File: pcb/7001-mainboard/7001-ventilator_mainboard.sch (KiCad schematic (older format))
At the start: 117 parts, among them J1 USB_B_Micro, J10 6-pin header, J11 4-pin screw terminal, J12 3-pin screw terminal, J13 2-pin screw terminal, J14 2-pin screw terminal, J15 2x10-pin header, J16 10-pin SWD header, J2 4-pin header, J3 2-pin screw terminal, J4 DNI, J5 2-pin screw terminal, J6 5V out, J7 2-pin screw terminal, J8 3-pin screw terminal, J9 Raspberry_Pi_2_3, U13 ITS4142NHUMA1, U14 ITS4142NHUMA1, U2 TPD2E2U06, U3 LPC11U37FBD48-401_, U4 MCP1825S-3302E, U5 S24SE05004PDFA_DC-DC, U6 LM2937IMP-12/NOPB, U7 AD5410AREZ, Y1 12MHz

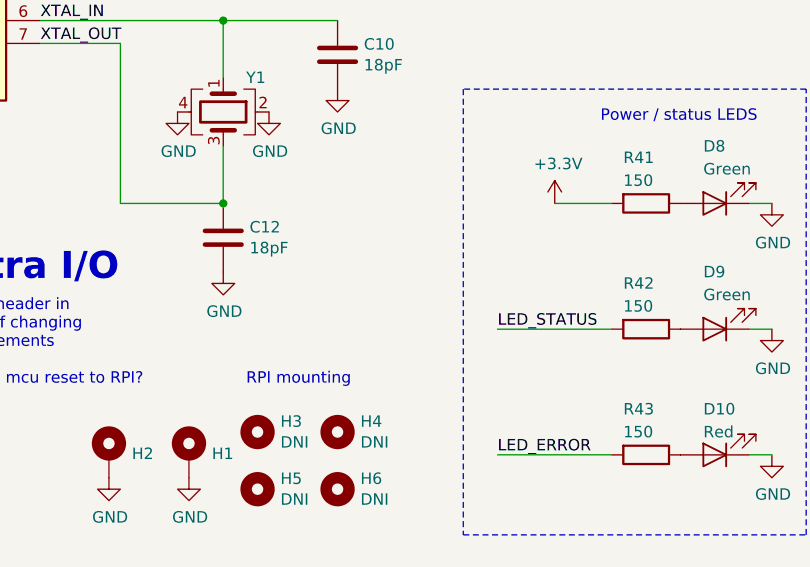
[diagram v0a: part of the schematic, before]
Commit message: Fix footprint bugs
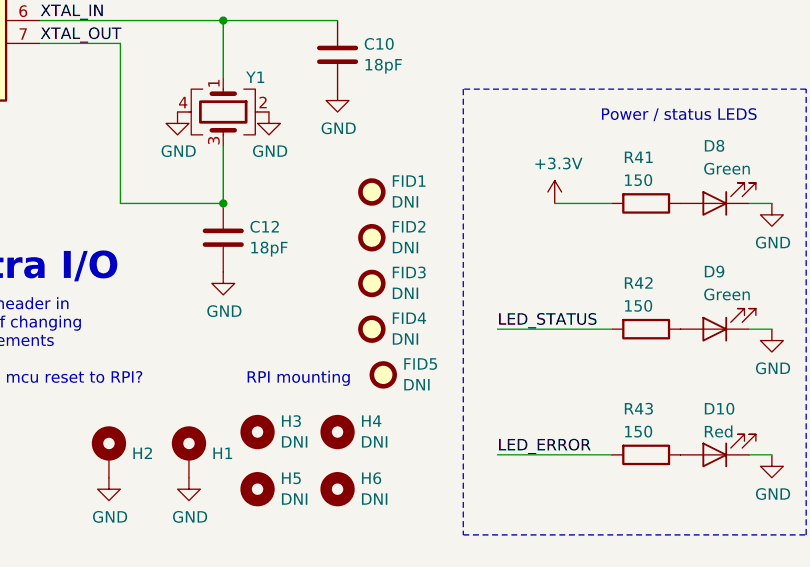
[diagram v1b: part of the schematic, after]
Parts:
- added FID1, FID2, FID3, FID4, FID5: DNI, Fiducial:Fiducial_1mm_Mask2mm, symbol Mechanical:Fiducial
- C22: footprint Jitter_Footprints:CP_Elec_12.5x13.5 -> Jitter_Footprints:CP_Elec_12.5_MAL214699107E3
- J1: footprint Connector_USB:USB_Micro-B_Molex_47346-0001 -> Jitter_Footprints:USB_Micro-B_Molex_47346-0001
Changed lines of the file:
@@
 F 0 "J1" H 1005 7117 50  0000 C CNN
 F 1 "USB_B_Micro" H 1005 7026 50  0000 C CNN
-F 2 "Connector_USB:USB_Micro-B_Molex_47346-0001" H 1100 6600 50  0001 C CNN
+F 2 "Jitter_Footprints:USB_Micro-B_Molex_47346-0001" H 1100 6600 50  0001 C CNN
 F 3 "~" H 1100 6600 50  0001 C CNN
 F 4 "47346-0001" H 950 6650 50  0001 C CNN "MPN"
@@
 F 0 "C22" H 5218 1596 50  0000 L CNN
 F 1 "330uF" H 5218 1505 50  0000 L CNN
-F 2 "Jitter_Footprints:CP_Elec_12.5x13.5" H 5138 1400 50  0001 C CNN
+F 2 "Jitter_Footprints:CP_Elec_12.5_MAL214699107E3" H 5138 1400 50  0001 C CNN
 F 3 "~" H 5100 1550 50  0001 C CNN
 F 4 "MAL214699107E3" H 5100 1550 50  0001 C CNN "MPN"
@@
 Wire Wire Line
 	5500 7050 6550 7050
+$Comp
+L Mechanical:Fiducial FID1
+U 1 1 610B1F93
+P 6950 9600
+F 0 "FID1" H 7035 9646 50  0000 L CNN
+F 1 "DNI" H 7035 9555 50  0000 L CNN
+F 2 "Fiducial:Fiducial_1mm_Mask2mm" H 6950 9600 50  0001 C CNN
+F 3 "~" H 6950 9600 50  0001 C CNN
+	1    6950 9600
+	1    0    0    -1
+$EndComp
+$Comp
+L Mechanical:Fiducial FID2
+U 1 1 610B21B1
+P 6950 9800
+F 0 "FID2" H 7035 9846 50  0000 L CNN
+F 1 "DNI" H 7035 9755 50  0000 L CNN
+F 2 "Fiducial:Fiducial_1mm_Mask2mm" H 6950 9800 50  0001 C CNN
+F 3 "~" H 6950 9800 50  0001 C CNN
+	1    6950 9800
+	1    0    0    -1
+$EndComp
+$Comp
+L Mechanical:Fiducial FID3
+U 1 1 610B2466
+P 6950 10000
+F 0 "FID3" H 7035 10046 50  0000 L CNN
+F 1 "DNI" H 7035 9955 50  0000 L CNN
+F 2 "Fiducial:Fiducial_1mm_Mask2mm" H 6950 10000 50  0001 C CNN
+F 3 "~" H 6950 10000 50  0001 C CNN
+	1    6950 10000
+	1    0    0    -1
+$EndComp
+$Comp
+L Mechanical:Fiducial FID4
+U 1 1 610B26BD
+P 6950 10200
+F 0 "FID4" H 7035 10246 50  0000 L CNN
+F 1 "DNI" H 7035 10155 50  0000 L CNN
+F 2 "Fiducial:Fiducial_1mm_Mask2mm" H 6950 10200 50  0001 C CNN
+F 3 "~" H 6950 10200 50  0001 C CNN
+	1    6950 10200
+	1    0    0    -1
+$EndComp
+$Comp
+L Mechanical:Fiducial FID5
+U 1 1 610BC399
+P 7000 10400
+F 0 "FID5" H 7085 10446 50  0000 L CNN
+F 1 "DNI" H 7085 10355 50  0000 L CNN
+F 2 "Fiducial:Fiducial_1mm_Mask2mm" H 7000 10400 50  0001 C CNN
+F 3 "~" H 7000 10400 50  0001 C CNN
+	1    7000 10400
+	1    0    0    -1
+$EndComp
 $EndSCHEMATC

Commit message: PCB: Finish layout
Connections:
- wire segments 350 -> 348
- no-connect marks 39 -> 40
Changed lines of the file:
@@
 Wire Wire Line
 	4100 7350 3050 7350
-Text Label 3050 8250 0    50   ~ 0
+Text Label 6550 7650 2    50   ~ 0
 PSENSE_1_DATA_READY
 Wire Wire Line
@@
 Text Label 9200 10750 0    50   ~ 0
 A_PRESSURE_1
+Text Label 3050 8050 0    50   ~ 0
+A_PRESSURE_1
+Wire Wire Line
+	3050 8050 4100 8050
 Text Label 3050 7950 0    50   ~ 0
-A_PRESSURE_1
-Wire Wire Line
-	3050 8050 4100 8050
-Text Label 3050 8050 0    50   ~ 0
 A_PRESSURE_2
 Text Label 9200 10850 0    50   ~ 0
@@
 Wire Wire Line
 	5500 7650 6550 7650
-Text Label 6550 7650 2    50   ~ 0
+Text Label 3050 8250 0    50   ~ 0
 PSENSE_2_SPI_~CS~
 Text Label 3600 8850 0    50   ~ 0
@@
 MCU_IO_1
 Wire Wire Line
-	3050 8650 4100 8650
-Wire Wire Line
-	3050 6850 4100 6850
-Wire Wire Line
 	3450 7100 3150 7100
 Wire Wire Line
@@
 Wire Wire Line
 	6550 6950 5500 6950
-NoConn ~ 3050 8650
+NoConn ~ 4100 8650
 Wire Wire Line
 	3050 8250 4100 8250
-NoConn ~ 3050 6850
+NoConn ~ 4100 6850
 NoConn ~ 5500 7550
 Text Label 3050 6750 2    50   ~ 0
@@
 	1    0    0    -1
 $EndComp
+NoConn ~ 4100 7250
 $EndSCHEMATC

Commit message: PCB: schematics for V2
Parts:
- removed D11, D5: D_TVS, Jitter_Footprints:WE-TVSP_TVS_DIODE, symbol Device:D_TVS
- removed J12, J8: 3-pin screw terminal, Jitter_Footprints:TerminalBlock_Wurth_WR-TBL_691322110003_1x03_P3.50mm_Horizontal, symbol Connector_Generic:Conn_01x03
- removed J2: 4-pin header, Connector_PinSocket_2.54mm:PinSocket_1x04_P2.54mm_Vertical, symbol Connector_Generic:Conn_01x04
- removed J4: DNI, Connector_PinHeader_2.54mm:PinHeader_1x03_P2.54mm_Vertical, symbol Connector_Generic:Conn_01x03
- removed J7: 2-pin screw terminal, Jitter_Footprints:TerminalBlock_Wurth_WR-TBL_691322110002_1x02_P3.50mm_Horizontal, symbol Connector_Generic:Conn_01x02
- removed JP1: 5V_jumper, Connector_PinHeader_2.54mm:PinHeader_1x03_P2.54mm_Vertical, symbol Jumper:Jumper_3_Bridged12
- removed R13: 0, Resistor_SMD:R_0805_2012Metric, symbol Device:R
- removed U6: LM2937IMP-12/NOPB, Package_TO_SOT_SMD:SOT-223-3_TabPin2, symbol Regulator_Linear:MCP1825S
- removed U7: AD5410AREZ, Jitter_Footprints:TSSOP-24-1EP_4.4x7.8mm_P0.65mm, symbol Jitter_Components:AD5410AREZ
- added D11: D_Schottky, Diode_SMD:D_SOD-123F, symbol Device:D_Schottky
- added D5: Green, LED_SMD:LED_0805_2012Metric, symbol Device:LED
- added FB1, FB2: BLM18HE601SN1D, Inductor_SMD:L_0603_1608Metric, symbol Device:Ferrite_Bead
- added J2, J4: 2-pin screw terminal, Jitter_Footprints:TerminalBlock_Wurth_WR-TBL_691322110002_1x02_P3.50mm_Horizontal, symbol Connector_Generic:Conn_01x02
- added J7: 6-pin FFC connector, Jitter_Footprints:Hirose_FH12-6S-0.5SH_1x06-1MP_P0.50mm_Horizontal, symbol Connector_Generic:Conn_01x06
- added J8: 2-pin screw terminal, Jitter_Footprints:TerminalBlock_Wurth_WR-TBL_691322110004_1x04_P3.50mm_Horizontal, symbol Connector_Generic:Conn_01x04
- added Q1: NX3020NAKV,115, Package_TO_SOT_SMD:SOT-666, symbol Device:Q_DUAL_NMOS_S1G1D2S2G2D1
- added R21: 4.7k, Resistor_SMD:R_0805_2012Metric, symbol Device:R
- added R44, R45, R46: 3.3k, Resistor_SMD:R_0805_2012Metric, symbol Device:R
- added R47, R49, R50: 150, Resistor_SMD:R_0805_2012Metric, symbol Device:R
- added R48: 2.2k, Resistor_SMD:R_0805_2012Metric, symbol Device:R
- added TP6, TP7: DNI, TestPoint:TestPoint_THTPad_D1.5mm_Drill0.7mm, symbol Connector:TestPoint
- added U15, U6: MCP4725, Package_TO_SOT_SMD:SOT-23-6, symbol Jitter_Components:MCP4725
- added U16: LD1086DT33TR, Package_TO_SOT_SMD:TO-252-2, symbol Regulator_Linear:LD1086DTTR
- added U7: ITS4142NHUMA1, Package_TO_SOT_SMD:SOT-223, symbol Jitter_Components:ITS4142NHUMA1
- C1, C15: purpose (none) -> decoupling
- C14: value 10uF -> 10uF 50V; footprint Capacitor_SMD:C_0805_2012Metric -> Capacitor_SMD:C_1210_3225Metric
- C20: value 100nF 50V -> 2.2nF; purpose (none) -> filter (see MPXH sensor datasheet)
- C21: value 10uF 50V -> 100nF; footprint Capacitor_SMD:C_1210_3225Metric -> Capacitor_SMD:C_0805_2012Metric; purpose (none) -> decoupling
- C23: value 10nF -> 100nF; purpose Iout slew rate limit: rise time 0.2ms @ 10nF -> decoupling
- C24, C41: value 100nF 50V -> 10uF 50V; footprint Capacitor_SMD:C_0805_2012Metric -> Capacitor_SMD:C_1210_3225Metric
- C26: value 100nF -> 10uF 50V; footprint Capacitor_SMD:C_0805_2012Metric -> Capacitor_SMD:C_1210_3225Metric
- C27: value 10nF -> 2.2nF 50V; purpose Iout slew rate limit: rise time 0.2ms @ 10nF -> EMC filter
- C40: value 100nF -> 2.2nF; purpose (none) -> filter (see MPXH sensor datasheet)
- C43: value 100nF -> 10uF
- C48: value 10nF -> 100nF 50V; purpose Iout slew rate limit: rise time 0.2ms @ 10nF -> (none)
- J11: value 4-pin screw terminal -> 2-pin screw terminal
- J6: footprint Connector_PinHeader_2.54mm:PinHeader_1x02_P2.54mm_Vertical -> Connector_PinHeader_2.54mm:PinHeader_1x05_P2.54mm_Vertical; symbol Connector_Generic:Conn_01x02 -> Connector_Generic:Conn_01x05
- R10: value 10k -> 68k; purpose (none) -> voltage divider: pressure to mcu (5V to 3V max)
- R11: value 0 -> 1k5
- R12: value 10k -> 1k5
- R14: value DNI -> 100k; purpose (none) -> voltage divider: pressure to mcu (5V to 3V max)
- R15: value 150 -> 10k; Reason Current-to-voltage scaling -> (none)
- R18: value 0 -> 10k
- R19, R37: value DNI -> 3.3k
- R31: value 3.3k -> 68k; Reason Voltage scaling: 10 to ca 3 -> (none); purpose (none) -> voltage divider: pressure to mcu (5V to 3V max)
- R32: value 10k -> 4.7k; Reason Voltage scaling: 10 to ca 3 -> (none)
- R33: value 0 -> 100k; purpose (none) -> voltage divider: pressure to mcu (5V to 3V max)
- R35: value 4.7k -> 10k
- R8, R9: value 1k5 -> 0
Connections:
- net labels added: A_MFC_FEEDBACK_AIR, A_MFC_FEEDBACK_O2, A_MFC_PRESSURE, A_PSENSE_3, EXHALE_PWM, EXHALE_VALVE, EXTRA_PWM, EXTRA_VALVE, FLOW_I2C_SCL, FLOW_I2C_SDA, I2C_3V3_SCL, I2C_3V3_SDA, I2C_5V_SCL, I2C_5V_SDA, INHALE_PWM, INHALE_VALVE, MFC_SETPOINT_AIR, MFC_SETPOINT_O2, POWER_STATUS, RPI_ON_OFF, RPI_~ISP~, RPI_~RST~, USER_SWITCH, V_flow_3v3, V_flow_heater
- net labels removed: +12V, 24V_SW1_OUT, 24V_SW2_OUT, A_FLOW, A_PREG_PRESSURE, A_PRESSURE_1, A_PRESSURE_2, DCDC_5V, I2C_SCL, I2C_SDA, I_PREG_FEEDBACK, I_PREG_SETPOINT, PREG_CLEAR, PREG_OK, PREG_SPI_CLK, PREG_SPI_MISO, PREG_SPI_MOSI, PREG_SPI_~CS~, RPI_IO_3, V_PU, switch_1_out, switch_2_out
- wire segments 348 -> 355
- no-connect marks 40 -> 39
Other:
- note added: "(boot_USB)"
- note added: "12-24V 6W 50mv rms"
- note added: "19.6V out:\nVo = 1.25 * (1+R2/R1)"
- note added: "24V -> 5V 3A"
- note added: "24V power input"
- note added: "24VDC 4A"
- note added: "2x Mass Flow Controller"
- note added: "3.3V -1%/+5%\n50mA 20mv rms"
- note added: "3x 24V Valve"
- note added: "5V -> 3.3V"
- note added: "5V power is provided\nfor the Raspberry Pi\nvia this connector.\nUART is also connected."
- note added: "ESD protection\nSee datasheet for layout"
- note added: "Extra header in\ncase of changing\nrequirements"
- note added: "Flow Sensor"
- note added: "HW_V1"
- note added: "I2C"
- note added: "ISP RX"
- note added: "ISP TX"
- note added: "Input filter + reverse polarity protection"
- note added: "MCU can\nwake-up\nthe RPI"
- note added: "Note:\nUSB is for debugging /\nmaintenance only\n"
- note added: "Override internal\npullup for ISP"
- note added: "Place close to\nADC input"
- note added: "Pulldown in MCU"
- note added: "RPI Connector"
- note added: "Signal will be connected by UPS relay\nSeries resistor for robustness + filtering"
- note added: "Soft on/off switch"
- note added: "Soft on/off switch:\nRC-network for debouncing"
- note added: "TODO BUZZER"
- note added: "TODO REMAP GPIOS"
- note added: "TODO REVIEW FOOTPRINT"
- note added: "TODO SETPOINT_OUT ESD/SURGE PROTECTION?\nTODO how many wires from MFC\nTODO which connector"
- note added: "TODO VERIFY\nFFC pinout\nmatches flow sensor"
- note added: "UPS status"
- note added: "Valves are driven with 24V PWM signal"
- note added: "~RESET~\nand ~ISP~\ncan be used\nby RPI to\nupdate MCU\nfirmware"
- note removed: "(USB boot)"
- note removed: "12VDC 25mA"
- note removed: "24V -> 12V LDO (40mA)"
- note removed: "24V 1.5A -> 5V3A"
- note removed: "24VDC 1.5A \nOUTPUT"
- note removed: "24VDC 3A"
- note removed: "2x 24V output"
- note removed: "3.3V LDO"
- note removed: "4-20mA -> 0.6-3.0V\nLowpass filter:\n10k, 10nF = 1.6kHz"
- note removed: "4-20mA DAC to control\nthe pressure regulator.\nThe regulator also gives\na feedback signal 4-20mA.\n\nThe feedback is not used\ndirectly for control, but\ncan be used as sanity check."
- note removed: "4-20mA input"
- note removed: "4-20mA output"
- note removed: "5V power is provided\nfor the Raspberry Pi\nvia this connector.\nUART is also connected.\n\nAs a fallback, the Pi\ncan use its own PSU and\nconnect via USB."
- note removed: "ESD protection\nSee datasheet for layout\n\nNote: USB is optional:\n- debugging (UART-over-USB)\n- raspberry pi (alt voor connector)\n"
- note removed: "Extra header in\ncase of changing\nrequirements\n\nTODO: mcu reset to RPI?"
- note removed: "Flow sensor (10V analog)"
- note removed: "I2C port"
- note removed: "Jumper Option:\n1-2: power 5V from 24V DC/DC\n2-3: power 5V from USB\nNC: power 5V from Raspberry Pi\n\nin production, this jumper\ncan be left out"
- note removed: "NOTE: LPC11u is 3.3V,\nbut 5v-tolerant for I2C;\noptional I2C-based flow sensors \nallow 2.5V as digital high;\npressure sensor is 3.3V-based,\nunknown if 5V-tolerant"
- note removed: "Note: do we need this?\nR6/R29 as DNI\nshould also enable\npower.."
- note removed: "Power Input"
- note removed: "Pressure regulator (RP200_C_???)\n"
- note removed: "RPI connector"
- note removed: "Scale 12V input to ca 3V\nLowpass fc ca 600Hz"
- note removed: "TODO:\n\n- test points?\n- fiducials"
- moved on the sheet: C10, C11, C12, C13, C16, C17, C18, C19, C2, C22, C25, C28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

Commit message: Fix bug in schematics
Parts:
- added H7: DNI (mounting hole), MountingHole:MountingHole_3.5mm_Pad_Via, symbol Mechanical:MountingHole_Pad
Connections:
- net GND: now also H7.1
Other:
- moved on the sheet: H1, H2
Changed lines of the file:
@@
 L Mechanical:MountingHole_Pad H1
 U 1 1 5C0E7FF6
-P 6100 10700
-F 0 "H1" H 6200 10705 50  0000 L CNN
-F 1 "DNI (mounting hole)" H 6200 10660 50  0001 L CNN
-F 2 "MountingHole:MountingHole_3.5mm_Pad_Via" H 6100 10700 50  0001 C CNN
-F 3 "~" H 6100 10700 50  0001 C CNN
-	1    6100 10700
+P 5350 10700
+F 0 "H1" H 5450 10705 50  0000 L CNN
+F 1 "DNI (mounting hole)" H 5450 10660 50  0001 L CNN
+F 2 "MountingHole:MountingHole_3.5mm_Pad_Via" H 5350 10700 50  0001 C CNN
+F 3 "~" H 5350 10700 50  0001 C CNN
+	1    5350 10700
 	1    0    0    -1
 $EndComp
@@
 L power:GND #PWR0119
 U 1 1 5C0E807D
-P 6100 10800
-F 0 "#PWR0119" H 6100 10550 50  0001 C CNN
-F 1 "GND" H 6105 10627 50  0000 C CNN
-F 2 "" H 6100 10800 50  0001 C CNN
-F 3 "" H 6100 10800 50  0001 C CNN
-	1    6100 10800
+P 5350 10800
+F 0 "#PWR0119" H 5350 10550 50  0001 C CNN
+F 1 "GND" H 5355 10627 50  0000 C CNN
+F 2 "" H 5350 10800 50  0001 C CNN
+F 3 "" H 5350 10800 50  0001 C CNN
+	1    5350 10800
 	1    0    0    -1
 $EndComp
@@
 L Mechanical:MountingHole_Pad H2
 U 1 1 5EAC584F
-P 5750 10700
-F 0 "H2" H 5850 10705 50  0000 L CNN
-F 1 "DNI (mounting hole)" H 5850 10660 50  0001 L CNN
-F 2 "MountingHole:MountingHole_3.5mm_Pad_Via" H 5750 10700 50  0001 C CNN
-F 3 "~" H 5750 10700 50  0001 C CNN
-	1    5750 10700
+P 5700 10700
+F 0 "H2" H 5800 10705 50  0000 L CNN
+F 1 "DNI (mounting hole)" H 5800 10660 50  0001 L CNN
+F 2 "MountingHole:MountingHole_3.5mm_Pad_Via" H 5700 10700 50  0001 C CNN
+F 3 "~" H 5700 10700 50  0001 C CNN
+	1    5700 10700
 	1    0    0    -1
 $EndComp
@@
 L power:GND #PWR022
 U 1 1 5EAC5855
-P 5750 10800
-F 0 "#PWR022" H 5750 10550 50  0001 C CNN
-F 1 "GND" H 5755 10627 50  0000 C CNN
-F 2 "" H 5750 10800 50  0001 C CNN
-F 3 "" H 5750 10800 50  0001 C CNN
-	1    5750 10800
+P 5700 10800
+F 0 "#PWR022" H 5700 10550 50  0001 C CNN
+F 1 "GND" H 5705 10627 50  0000 C CNN
+F 2 "" H 5700 10800 50  0001 C CNN
+F 3 "" H 5700 10800 50  0001 C CNN
+	1    5700 10800
 	1    0    0    -1
 $EndComp
@@
 NoConn ~ 5450 8100
 NoConn ~ 5900 2450
+$Comp
+L Mechanical:MountingHole_Pad H7
+U 1 1 6140C98B
+P 6050 10700
+F 0 "H7" H 6150 10705 50  0000 L CNN
+F 1 "DNI (mounting hole)" H 6150 10660 50  0001 L CNN
+F 2 "MountingHole:MountingHole_3.5mm_Pad_Via" H 6050 10700 50  0001 C CNN
+F 3 "~" H 6050 10700 50  0001 C CNN
+	1    6050 10700
+	1    0    0    -1
+$EndComp
+$Comp
+L power:GND #PWR0171
+U 1 1 6140C991
+P 6050 10800
+F 0 "#PWR0171" H 6050 10550 50  0001 C CNN
+F 1 "GND" H 6055 10627 50  0000 C CNN
+F 2 "" H 6050 10800 50  0001 C CNN
+F 3 "" H 6050 10800 50  0001 C CNN
+	1    6050 10800
+	1    0    0    -1
+$EndComp
 $EndSCHEMATC

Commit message: Update schematics (PSU connector) + BOM
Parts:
- removed J2: 2-pin screw terminal, Jitter_Footprints:TerminalBlock_Wurth_WR-TBL_691322110002_1x02_P3.50mm_Horizontal, symbol Connector_Generic:Conn_01x02
- removed J8: 2-pin screw terminal, Jitter_Footprints:TerminalBlock_Wurth_WR-TBL_691322110004_1x04_P3.50mm_Horizontal, symbol Connector_Generic:Conn_01x04
- added C50: 100nF, Capacitor_SMD:C_0805_2012Metric, symbol Device:C
- added J8: 2-pin screw terminal, Jitter_Footprints:TerminalBlock_Wurth_WR-TBL_691322110005_1x05_P3.50mm_Horizontal, symbol Connector_Generic:Conn_01x05
- added R22, R23: 1k5, Resistor_SMD:R_0805_2012Metric, symbol Device:R
- J11: footprint Jitter_Footprints:TerminalBlock_Wurth_WR-TBL_691322110004_1x04_P3.50mm_Horizontal -> Jitter_Footprints:TerminalBlock_Wurth_WR-TBL_691322110005_1x05_P3.50mm_Horizontal; symbol Connector_Generic:Conn_01x04 -> Connector_Generic:Conn_01x05; Farnell 1841317 -> 1841318; MPN 691322110004 -> 691322110005
- J5: footprint Jitter_Footprints:TerminalBlock_Wurth_WR-TBL_691322110002_1x02_P3.50mm_Horizontal -> Jitter_Footprints:TerminalBlock_Wurth_WR-TBL_691322110008_1x08_P3.50mm_Horizontal; symbol Connector_Generic:Conn_01x02 -> Connector_Generic:Conn_01x08; Farnell 1841315 -> (none); MPN 691322110002 -> 691322110008
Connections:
- net +24V: now also J11.5 (Pin_5), J8.5 (Pin_5); no longer J11.4 (Pin_4)
- net +3V3: now also R23.2
- net GND: now also J11.4 (Pin_4), J5.1 (Pin_1), J5.2 (Pin_2), C50.2, J8.1 (Pin_1), J8.4 (Pin_4)
- net MFC_SETPOINT_O2: now also J8.3 (Pin_3)
- net PSENSE_RESET: now also U3.24 (PIO1_28); no longer U3.13 (PIO1_20)
- net at R11.1: now also J5.6 (Pin_6)
- net at R12.1: now also J5.5 (Pin_5)
- net at C46.2, D4.1 (A1), FL1.1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: now also J5.3 (Pin_3); no longer J5.1 (Pin_1)
- net at C46.1, D4.2 (A2), FL1.2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: now also J5.4 (Pin_4); no longer J5.2 (Pin_2)
- net at R10.2: now also J8.2 (Pin_2)
- net POWER_STATUS renamed POWER_STATUS_DISCHARGING
- net POWER_STATUS_DISCHARGING: now also U3.13 (PIO1_20); no longer U3.12 (PIO1_27)
- new net: J5.7 (Pin_7), R22.1
- new net: J5.8 (Pin_8), R23.1
- new net POWER_STATUS_FAIL: C50.1, R22.2, U3.12 (PIO1_27)
- no-connect marks 39 -> 38
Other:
- note added: "BATT_DISCHG"
- note added: "BATT_FAIL"
- note added: "PSU_EARTH"
- note added: "TODO Earth:\ndirectly to GND?"
- note added: "TODO SETPOINT_OUT robustness:\nESD/SURGE PROTECTION?"
- note added: "[0-5V]"
- note removed: "TODO SETPOINT_OUT ESD/SURGE PROTECTION?\nTODO how many wires from MFC\nTODO which connector"
- note removed: "UPS status"
- moved on the sheet: C10, C11, C12, C13, C14, C15, C16, C18, C2, C21, C22, C24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

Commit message: PCB: layout in progress
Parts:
- J5: Farnell (none) -> 1841314; MPN 691322110008 -> 691321100008
- J7: symbol Connector_Generic:Conn_01x06 -> Connector_Generic_MountingPin:Conn_01x06_MountingPin
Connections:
- net GND: now also J7.MP (MountPin)
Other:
- note added: "NOTE: this is \na vertical\nheader!\n3D Footprint\nis wrong.."
- note added: "TODO 6-pins?"
- note added: "TODO BUZZER(?)"
- note added: "TODO REMAP GPIOS\nfor easier routing"
- note removed: "TODO BUZZER"
- note removed: "TODO REMAP GPIOS"
- moved on the sheet: C49, J10, J15, J16

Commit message: PCB layout: position of components near-final
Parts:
- added C51, C54: 100nF 50V, Capacitor_SMD:C_0805_2012Metric, symbol Device:C
- added C52: 1uF, Capacitor_SMD:C_0805_2012Metric, symbol Device:C
- added C53: 10uF, Capacitor_SMD:C_0805_2012Metric, symbol Device:C
- added J2: 6-pin FFC connector, Jitter_Footprints:Hirose_FH12-6S-0.5SH_1x06-1MP_P0.50mm_Horizontal, symbol Connector_Generic_MountingPin:Conn_01x06_MountingPin
- added R24: 1k5, Resistor_SMD:R_0805_2012Metric, symbol Device:R
- C43: value 10uF -> 100nF; purpose (none) -> decoupling
- R11: value 1k5 -> 10k
- R47: value 150 -> 150 1%
- R48: value 2.2k -> 2.32k 1%; Purpose (none) -> feedback divider: Vout ~20.5V
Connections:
- net +24V: now also R11.2
- net +3V3: now also C52.1; no longer C43.1, R11.2
- net FLOW_I2C_SCL: now also J2.4 (Pin_4)
- net FLOW_I2C_SDA: now also J2.3 (Pin_3)
- net GND: now also C51.2, C52.2, C53.2, C54.2, J2.2 (Pin_2), J2.5 (Pin_5), J2.MP (MountPin), R24.1
- net LED_ERROR: now also U3.17 (PIO0_21); no longer U3.42 (PIO0_23)
- net V_flow_3v3: now also C53.1, C54.1, J2.1 (Pin_1)
- net V_flow_heater: now also C51.1, J2.6 (Pin_6)
- net at J5.6 (Pin_6): now also J5.8 (Pin_8), R23.1; no longer R11.1
- new net BATT_LEVEL: C43.1, R11.1, R24.2, U3.42 (PIO0_23)
- no-connect marks 38 -> 37
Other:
- note added: "20.6V out:\nVo = 1.25 * (1+R2/R1)"
- note added: "2x Flow Sensor"
- note added: "Battery level\nto MCU"
- note added: "Required:\n- 12-24V 6W 50mv rms\n- 3.3V 25mv rms"
- note added: "Soft on/off\nswitch:\nRC-network\nfor debouncing"
- note added: "TODO REVIEW FOOTPRINT\nNOTE: LDO may run hot!"
- note removed: "(adc capable)"
- note removed: "12-24V 6W 50mv rms"
- note removed: "19.6V out:\nVo = 1.25 * (1+R2/R1)"
- note removed: "Flow Sensor"
- note removed: "Soft on/off switch:\nRC-network for debouncing"
- note removed: "TODO REVIEW FOOTPRINT"
- moved on the sheet: C19, C38, C41, C49, D10, D8, D9, FB1, FID1, FID2, FID3, FID4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
